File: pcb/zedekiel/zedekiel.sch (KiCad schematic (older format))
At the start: 150 parts, among them J2 USB_C_Receptacle_USB2.0, K1 KEYSW, K10 KEYSW, K11 KEYSW, K12 KEYSW, K13 KEYSW, K14 KEYSW, K15 KEYSW, K16 KEYSW, K17 KEYSW, K18 KEYSW, K19 KEYSW, K2 KEYSW, K20 KEYSW, K21 KEYSW, K22 KEYSW, K23 KEYSW, K24 KEYSW, K25 KEYSW, K26 KEYSW, K27 KEYSW, K28 KEYSW, K29 KEYSW, K3 KEYSW, K30 KEYSW, K31 KEYSW, K32 KEYSW, K33 KEYSW, K34 KEYSW, K35 KEYSW, K36 KEYSW, K37 KEYSW, K38 KEYSW, K39 KEYSW, K4 KEYSW, K40 KEYSW, K41 KEYSW, K42 KEYSW, K43 KEYSW, K44 KEYSW, K45 KEYSW, K46 KEYSW, K47 KEYSW, K48 KEYSW, K49 KEYSW, K5 KEYSW, K50 KEYSW, K51 KEYSW, K52 KEYSW, K53 KEYSW, K54 KEYSW, K55 KEYSW, K56 KEYSW, K57 KEYSW, K58 KEYSW, K59 KEYSW, K6 KEYSW, K60 KEYSW, K61 KEYSW, K62 KEYSW, K63 KEYSW, K64 KEYSW, K65 KEYSW, K66 KEYSW, K7 KEYSW, K8 KEYSW, K9 KEYSW, SW1 SW_PUSH, U1 ATmega16U4-AU_(modified), X1 16MHz

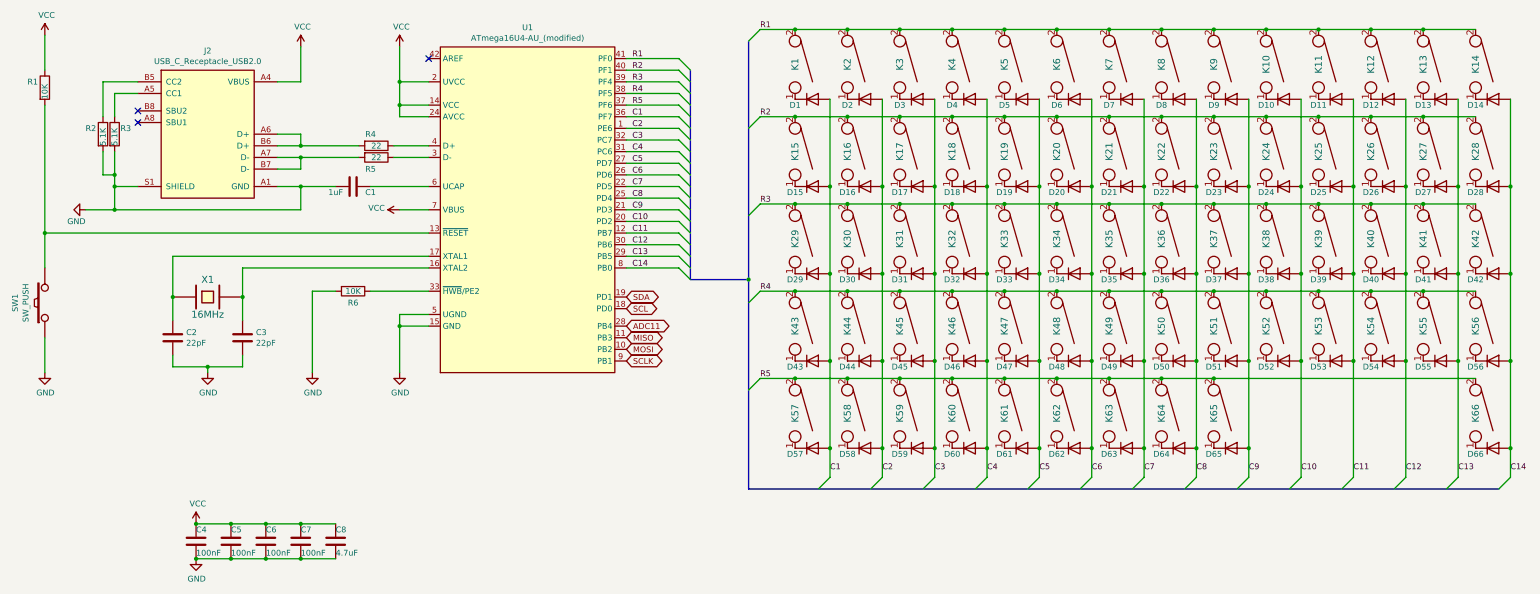
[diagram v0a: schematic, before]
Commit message: Diodes and sockets in place
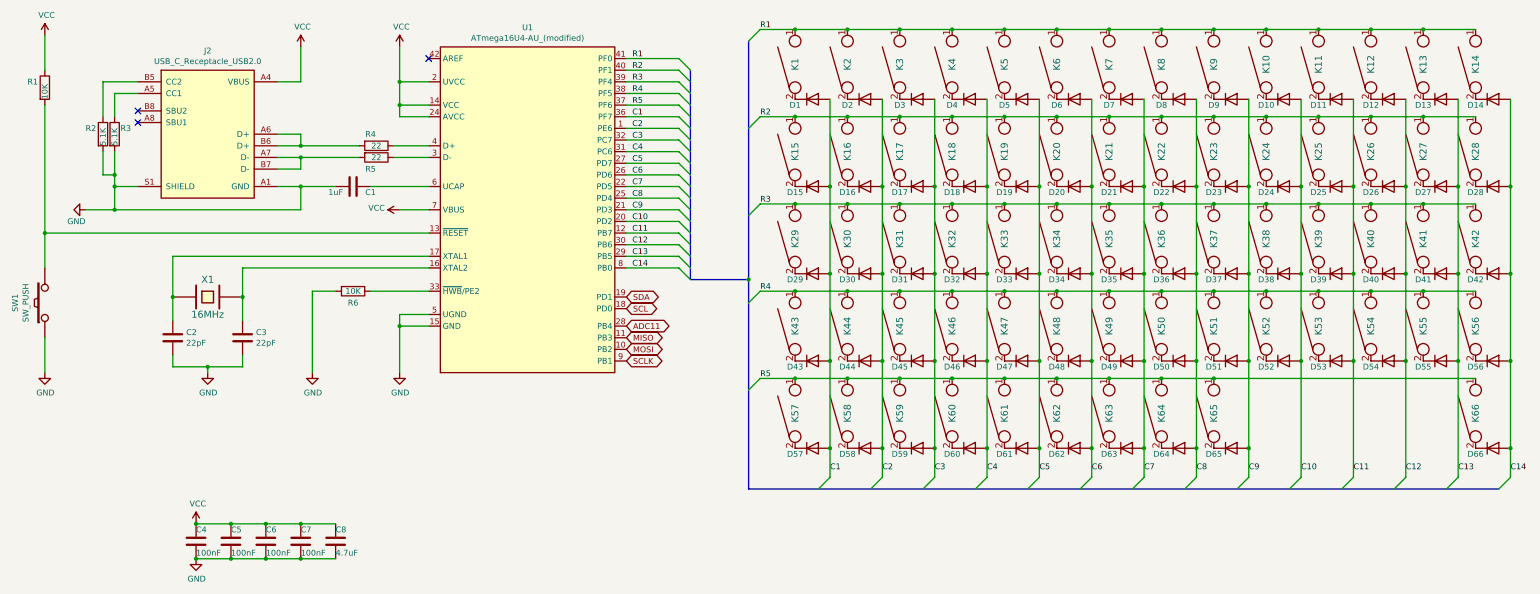
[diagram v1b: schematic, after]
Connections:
- net R1: now also K1.1, K10.1, K11.1, K12.1, K13.1, K14.1, K2.1, K3.1, K4.1, K5.1, K6.1, K7.1, K8.1, K9.1; no longer K1.2, K10.2, K11.2, K12.2, K13.2, K14.2, K2.2, K3.2, K4.2, K5.2, K6.2, K7.2, K8.2, K9.2
- net R2: now also K15.1, K16.1, K17.1, K18.1, K19.1, K20.1, K21.1, K22.1, K23.1, K24.1, K25.1, K26.1, K27.1, K28.1; no longer K15.2, K16.2, K17.2, K18.2, K19.2, K20.2, K21.2, K22.2, K23.2, K24.2, K25.2, K26.2, K27.2, K28.2
- net R3: now also K29.1, K30.1, K31.1, K32.1, K33.1, K34.1, K35.1, K36.1, K37.1, K38.1, K39.1, K40.1, K41.1, K42.1; no longer K29.2, K30.2, K31.2, K32.2, K33.2, K34.2, K35.2, K36.2, K37.2, K38.2, K39.2, K40.2, K41.2, K42.2
- net R4: now also K43.1, K44.1, K45.1, K46.1, K47.1, K48.1, K49.1, K50.1, K51.1, K52.1, K53.1, K54.1, K55.1, K56.1; no longer K43.2, K44.2, K45.2, K46.2, K47.2, K48.2, K49.2, K50.2, K51.2, K52.2, K53.2, K54.2, K55.2, K56.2
- net R5: now also K57.1, K58.1, K59.1, K60.1, K61.1, K62.1, K63.1, K64.1, K65.1, K66.1; no longer K57.2, K58.2, K59.2, K60.2, K61.2, K62.2, K63.2, K64.2, K65.2, K66.2
- net at D1.1 (K): now also K1.2; no longer K1.1
- net at D2.1 (K): now also K2.2; no longer K2.1
- net at D3.1 (K): now also K3.2; no longer K3.1
- net at D4.1 (K): now also K4.2; no longer K4.1
- net at D5.1 (K): now also K5.2; no longer K5.1
- net at D6.1 (K): now also K6.2; no longer K6.1
- net at D7.1 (K): now also K7.2; no longer K7.1
- net at D8.1 (K): now also K8.2; no longer K8.1
- net at D9.1 (K): now also K9.2; no longer K9.1
- net at D10.1 (K): now also K10.2; no longer K10.1
- net at D11.1 (K): now also K11.2; no longer K11.1
- net at D12.1 (K): now also K12.2; no longer K12.1
- net at D13.1 (K): now also K13.2; no longer K13.1
- net at D14.1 (K): now also K14.2; no longer K14.1
- net at D15.1 (K): now also K15.2; no longer K15.1
- net at D16.1 (K): now also K16.2; no longer K16.1
- net at D17.1 (K): now also K17.2; no longer K17.1
- net at D18.1 (K): now also K18.2; no longer K18.1
- net at D19.1 (K): now also K19.2; no longer K19.1
- net at D20.1 (K): now also K20.2; no longer K20.1
- net at D21.1 (K): now also K21.2; no longer K21.1
- net at D22.1 (K): now also K22.2; no longer K22.1
- net at D23.1 (K): now also K23.2; no longer K23.1
- net at D24.1 (K): now also K24.2; no longer K24.1
- net at D25.1 (K): now also K25.2; no longer K25.1
- net at D26.1 (K): now also K26.2; no longer K26.1
- net at D27.1 (K): now also K27.2; no longer K27.1
- net at D28.1 (K): now also K28.2; no longer K28.1
- net at D29.1 (K): now also K29.2; no longer K29.1
- net at D30.1 (K): now also K30.2; no longer K30.1
- net at D31.1 (K): now also K31.2; no longer K31.1
- net at D32.1 (K): now also K32.2; no longer K32.1
- net at D33.1 (K): now also K33.2; no longer K33.1
- net at D34.1 (K): now also K34.2; no longer K34.1
- net at D35.1 (K): now also K35.2; no longer K35.1
- net at D36.1 (K): now also K36.2; no longer K36.1
- net at D37.1 (K): now also K37.2; no longer K37.1
- net at D38.1 (K): now also K38.2; no longer K38.1
- net at D39.1 (K): now also K39.2; no longer K39.1
- net at D40.1 (K): now also K40.2; no longer K40.1
- net at D41.1 (K): now also K41.2; no longer K41.1
- net at D42.1 (K): now also K42.2; no longer K42.1
- net at D43.1 (K): now also K43.2; no longer K43.1
- net at D44.1 (K): now also K44.2; no longer K44.1
- net at D45.1 (K): now also K45.2; no longer K45.1
- net at D46.1 (K): now also K46.2; no longer K46.1
- net at D47.1 (K): now also K47.2; no longer K47.1
- net at D48.1 (K): now also K48.2; no longer K48.1
- net at D49.1 (K): now also K49.2; no longer K49.1
- net at D50.1 (K): now also K50.2; no longer K50.1
- net at D51.1 (K): now also K51.2; no longer K51.1
- net at D52.1 (K): now also K52.2; no longer K52.1
- net at D53.1 (K): now also K53.2; no longer K53.1
- net at D54.1 (K): now also K54.2; no longer K54.1
- net at D55.1 (K): now also K55.2; no longer K55.1
- net at D56.1 (K): now also K56.2; no longer K56.1
- net at D57.1 (K): now also K57.2; no longer K57.1
- net at D58.1 (K): now also K58.2; no longer K58.1
- net at D59.1 (K): now also K59.2; no longer K59.1
- net at D60.1 (K): now also K60.2; no longer K60.1
- net at D61.1 (K): now also K61.2; no longer K61.1
- net at D62.1 (K): now also K62.2; no longer K62.1
- net at D63.1 (K): now also K63.2; no longer K63.1
- net at D64.1 (K): now also K64.2; no longer K64.1
- net at D65.1 (K): now also K65.2; no longer K65.1
- net at D66.1 (K): now also K66.2; no longer K66.1
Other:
- moved on the sheet: K1, K10, K11, K12, K13, K14, K15, K16, K17, K18, K19, K2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

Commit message: Holes and stabilizers
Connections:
- net C1: no longer D57.2 (A)
- net C10: now also D62.2 (A)
- net C11: now also D63.2 (A)
- net C12: now also D64.2 (A)
- net C13: now also D65.2 (A)
- net C2: now also D57.2 (A); no longer D58.2 (A)
- net C3: no longer D59.2 (A)
- net C4: now also D58.2 (A); no longer D60.2 (A)
- net C5: now also D59.2 (A); no longer D61.2 (A)
- net C6: no longer D62.2 (A)
- net C7: now also D60.2 (A); no longer D63.2 (A)
- net C8: now also D61.2 (A); no longer D64.2 (A)
- net C9: no longer D65.2 (A)
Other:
- moved on the sheet: D57, D58, D59, D60, D61, D62, D63, D64, D65, K57, K58, K59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

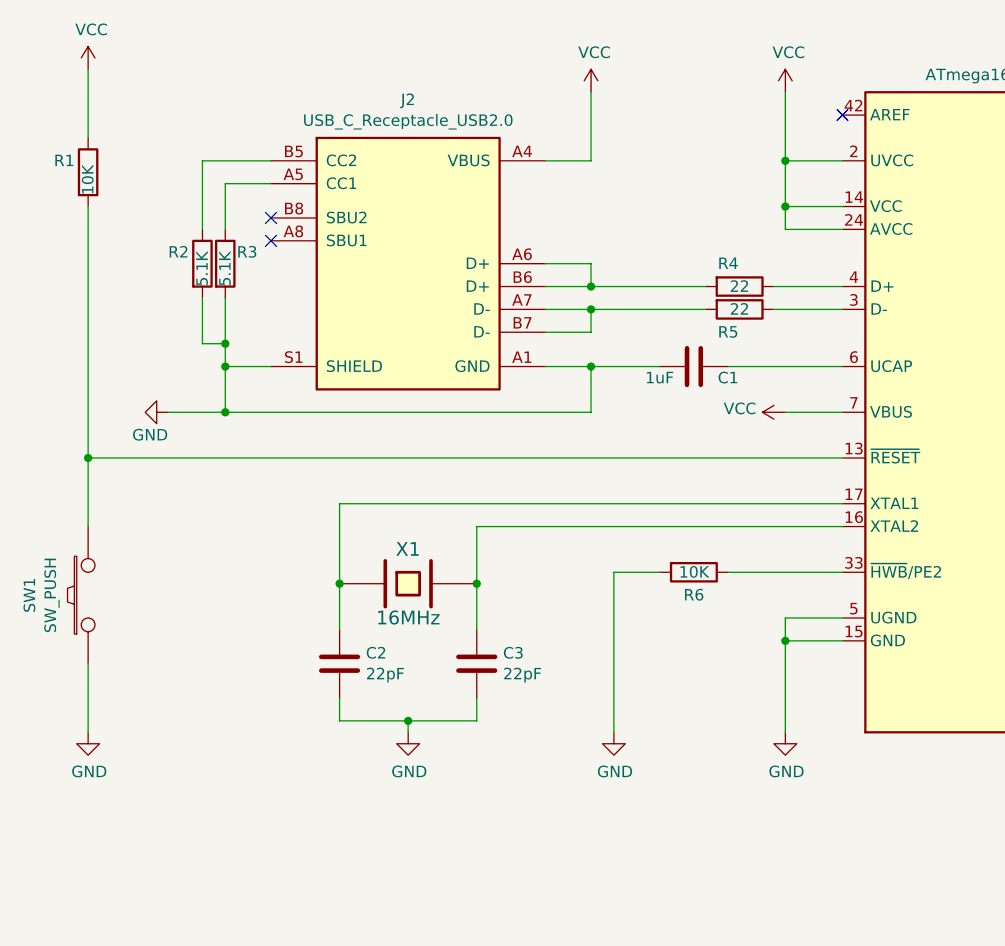
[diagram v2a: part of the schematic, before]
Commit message: Routing started.
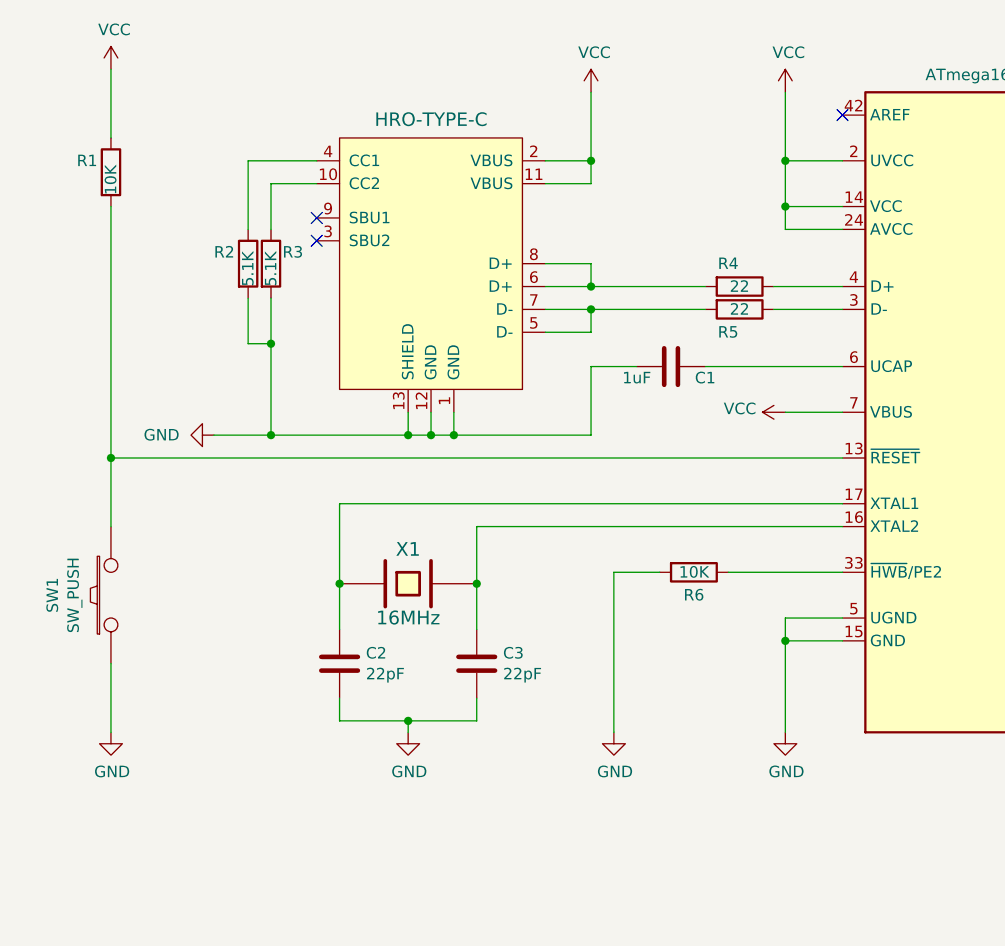
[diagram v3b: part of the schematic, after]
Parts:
- removed J2: USB_C_Receptacle_USB2.0, Connectors_USB:USB_C_Receptacle_Amphenol_12401548E4-2A, symbol usb_c_receptacle_usb2.0_modified:USB_C_Receptacle_USB2.0
- added USB?: HRO-TYPE-C, symbol hro-type-c_modified:HRO-TYPE-C
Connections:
- net GND: now also USB?.1 (GND), USB?.12 (GND), USB?.13 (SHIELD)
- net VCC: now also USB?.11 (VBUS), USB?.2 (VBUS)
- net at R3.1: now also USB?.10 (CC2)
- net at R2.1: now also USB?.4 (CC1)
- net at R4.2: now also USB?.6 (D+), USB?.8 (D+)
- net at R5.2: now also USB?.5 (D-), USB?.7 (D-)
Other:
- moved on the sheet: C1, R1, R2, R3, SW1
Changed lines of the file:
@@
 L Device:C C1
 U 1 1 5EE5A2F4
-P 3900 2450
-F 0 "C1" V 3950 2600 50  0000 C CNN
-F 1 "1uF" V 3950 2300 50  0000 C CNN
-F 2 "Capacitors_SMD:C_0603" H 3938 2300 50  0001 C CNN
-F 3 "~" H 3900 2450 50  0001 C CNN
-	1    3900 2450
+P 3800 2450
+F 0 "C1" V 3850 2600 50  0000 C CNN
+F 1 "1uF" V 3850 2300 50  0000 C CNN
+F 2 "Capacitors_SMD:C_0603" H 3838 2300 50  0001 C CNN
+F 3 "~" H 3800 2450 50  0001 C CNN
+	1    3800 2450
 	0    1    1    0
 $EndComp
 Wire Wire Line
-	4050 2450 4550 2450
-Wire Wire Line
-	3750 2450 3450 2450
-Wire Wire Line
-	3450 2650 3450 2450
-Connection ~ 3450 2450
-Wire Wire Line
-	3450 2450 3250 2450
+	3950 2450 4550 2450
 $Comp
 L keyboard_parts:SW_PUSH SW1
 U 1 1 5EE97D58
-P 1250 3450
-F 0 "SW1" H 1250 3705 50  0000 C CNN
-F 1 "SW_PUSH" H 1250 3614 50  0000 C CNN
-F 2 "custom:pad-button" H 1250 3450 60  0001 C CNN
-F 3 "" H 1250 3450 60  0000 C CNN
-	1    1250 3450
-	0    -1   -1   0
-$EndComp
-Wire Wire Line
-	1250 2850 1250 3150
+P 1350 3450
+F 0 "SW1" H 1350 3705 50  0000 C CNN
+F 1 "SW_PUSH" H 1350 3614 50  0000 C CNN
+F 2 "custom:pad-button" H 1350 3450 60  0001 C CNN
+F 3 "" H 1350 3450 60  0000 C CNN
+	1    1350 3450
+	0    -1   -1   0
+$EndComp
 $Comp
 L power:GND #PWR05
 U 1 1 5EEA1F4F
-P 1250 4050
-F 0 "#PWR05" H 1250 3800 50  0001 C CNN
-F 1 "GND" H 1255 3877 50  0000 C CNN
-F 2 "" H 1250 4050 50  0001 C CNN
-F 3 "" H 1250 4050 50  0001 C CNN
-	1    1250 4050
-	1    0    0    -1
-$EndComp
-Wire Wire Line
-	1250 3750 1250 4050
+P 1350 4050
+F 0 "#PWR05" H 1350 3800 50  0001 C CNN
+F 1 "GND" H 1355 3877 50  0000 C CNN
+F 2 "" H 1350 4050 50  0001 C CNN
+F 3 "" H 1350 4050 50  0001 C CNN
+	1    1350 4050
+	1    0    0    -1
+$EndComp
+Wire Wire Line
+	1350 3750 1350 4050
 $Comp
 L power:VCC #PWR01
 U 1 1 5EEA4CAF
-P 1250 1150
-F 0 "#PWR01" H 1250 1000 50  0001 C CNN
-F 1 "VCC" H 1265 1323 50  0000 C CNN
-F 2 "" H 1250 1150 50  0001 C CNN
-F 3 "" H 1250 1150 50  0001 C CNN
-	1    1250 1150
+P 1350 1150
+F 0 "#PWR01" H 1350 1000 50  0001 C CNN
+F 1 "VCC" H 1365 1323 50  0000 C CNN
+F 2 "" H 1350 1150 50  0001 C CNN
+F 3 "" H 1350 1150 50  0001 C CNN
+	1    1350 1150
 	1    0    0    -1
 $EndComp
@@
 L Device:R R1
 U 1 1 5EEB521E
-P 1250 1600
-F 0 "R1" H 1100 1650 50  0000 L CNN
-F 1 "10K" V 1250 1500 50  0000 L CNN
-F 2 "Resistors_SMD:R_0603" V 1180 1600 50  0001 C CNN
-F 3 "~" H 1250 1600 50  0001 C CNN
-	1    1250 1600
-	1    0    0    -1
-$EndComp
-Wire Wire Line
-	1250 1750 1250 2850
-Wire Wire Line
-	1250 1450 1250 1150
+P 1350 1600
+F 0 "R1" H 1200 1650 50  0000 L CNN
+F 1 "10K" V 1350 1500 50  0000 L CNN
+F 2 "Resistors_SMD:R_0603" V 1280 1600 50  0001 C CNN
+F 3 "~" H 1350 1600 50  0001 C CNN
+	1    1350 1600
+	1    0    0    -1
+$EndComp
+Wire Wire Line
+	1350 1450 1350 1150
 $Comp
 L power:GND #PWR04
 U 1 1 5EE60D7B
-P 1600 2650
-F 0 "#PWR04" H 1600 2400 50  0001 C CNN
-F 1 "GND" V 1700 2650 50  0000 R CNN
-F 2 "" H 1600 2650 50  0001 C CNN
-F 3 "" H 1600 2650 50  0001 C CNN
-	1    1600 2650
+P 1800 2750
+F 0 "#PWR04" H 1800 2500 50  0001 C CNN
+F 1 "GND" V 1800 2600 50  0000 R CNN
+F 2 "" H 1800 2750 50  0001 C CNN
+F 3 "" H 1800 2750 50  0001 C CNN
+	1    1800 2750
 	0    1    1    0
 $EndComp
@@
 	0    1    1    0
 $EndComp
-Connection ~ 1250 2850
-Wire Wire Line
-	1250 2850 4550 2850
 $Comp
 L power:GND #PWR06
@@
 Wire Wire Line
 	3450 5650 3150 5650
-$Comp
-L usb_c_receptacle_usb2.0_modified:USB_C_Receptacle_USB2.0 J2
-U 1 1 6061B4FB
-P 2650 2000
-F 0 "J2" H 2650 2717 50  0000 C CNN
-F 1 "USB_C_Receptacle_USB2.0" H 2650 2626 50  0000 C CNN
-F 2 "Connectors_USB:USB_C_Receptacle_Amphenol_12401548E4-2A" H 2800 1850 50  0001 C CNN
-F 3 "https://www.usb.org/sites/default/files/documents/usb_type-c.zip" H 2800 1850 50  0001 C CNN
-	1    2650 2000
-	1    0    0    -1
-$EndComp
-Wire Wire Line
-	2050 1550 1750 1550
-Wire Wire Line
-	2050 1650 1850 1650
-NoConn ~ 2050 1800
-NoConn ~ 2050 1900
-Wire Wire Line
-	3250 2000 3450 2000
-Wire Wire Line
-	3450 2000 3450 2100
-Wire Wire Line
-	3450 2100 3250 2100
+Wire Wire Line
+	2250 1550 1950 1550
+Wire Wire Line
+	2250 1650 2050 1650
+NoConn ~ 2250 1800
+NoConn ~ 2250 1900
 Wire Wire Line
 	3250 2200 3450 2200
@@
 	3450 2200 3950 2200
 Connection ~ 3450 2200
-Wire Wire Line
-	3950 2100 3450 2100
-Connection ~ 3450 2100
 Wire Wire Line
 	3250 1550 3450 1550
@@
 $EndComp
 Wire Wire Line
-	1750 1550 1750 1850
+	1950 1550 1950 1850
 $Comp
 L Device:R R2
 U 1 1 5EE7E2CD
-P 1750 2000
-F 0 "R2" H 1600 2050 50  0000 L CNN
-F 1 "5.1K" V 1750 1900 50  0000 L CNN
-F 2 "Resistors_SMD:R_0603" V 1680 2000 50  0001 C CNN
-F 3 "~" H 1750 2000 50  0001 C CNN
-	1    1750 2000
-	1    0    0    -1
-$EndComp
-Wire Wire Line
-	1850 1650 1850 1850
+P 1950 2000
+F 0 "R2" H 1800 2050 50  0000 L CNN
+F 1 "5.1K" V 1950 1900 50  0000 L CNN
+F 2 "Resistors_SMD:R_0603" V 1880 2000 50  0001 C CNN
+F 3 "~" H 1950 2000 50  0001 C CNN
+	1    1950 2000
+	1    0    0    -1
+$EndComp
+Wire Wire Line
+	2050 1650 2050 1850
 $Comp
 L Device:R R3
 U 1 1 5EE7DBB6
-P 1850 2000
-F 0 "R3" H 1900 2050 50  0000 L CNN
-F 1 "5.1K" V 1850 1900 50  0000 L CNN
-F 2 "Resistors_SMD:R_0603" V 1780 2000 50  0001 C CNN
-F 3 "~" H 1850 2000 50  0001 C CNN
-	1    1850 2000
-	1    0    0    -1
-$EndComp
-Wire Wire Line
-	1850 2150 1850 2350
-Wire Wire Line
-	1750 2150 1750 2350
-Wire Wire Line
-	1750 2350 1850 2350
-Wire Wire Line
-	2050 2450 1850 2450
-Wire Wire Line
-	1850 2450 1850 2650
-Connection ~ 1850 2650
-Wire Wire Line
-	1850 2650 3450 2650
-Wire Wire Line
-	1850 2350 1850 2450
-Connection ~ 1850 2350
-Connection ~ 1850 2450
-Wire Wire Line
-	1850 2650 1600 2650
+P 2050 2000
+F 0 "R3" H 2100 2050 50  0000 L CNN
+F 1 "5.1K" V 2050 1900 50  0000 L CNN
+F 2 "Resistors_SMD:R_0603" V 1980 2000 50  0001 C CNN
+F 3 "~" H 2050 2000 50  0001 C CNN
+	1    2050 2000
+	1    0    0    -1
+$EndComp
+Wire Wire Line
+	2050 2150 2050 2350
+Wire Wire Line
+	1950 2150 1950 2350
+Wire Wire Line
+	1950 2350 2050 2350
+Connection ~ 2050 2350
 $Comp
 L keyboard_parts:KEYSW K12
@@
 Wire Wire Line
 	9500 4100 10400 4100
+Connection ~ 3450 2100
+Wire Wire Line
+	3950 2100 3450 2100
+Wire Wire Line
+	3450 2100 3250 2100
+Wire Wire Line
+	3450 2000 3450 2100
+Wire Wire Line
+	3250 2000 3450 2000
+$Comp
+L hro-type-c_modified:HRO-TYPE-C USB?
+U 1 1 5EF51AB7
+P 3150 2050
+F 0 "USB?" H 2750 2050 60  0001 C CNN
+F 1 "HRO-TYPE-C" H 2750 2730 59  0000 C CNN
+F 2 "" H 3150 2050 60  0001 C CNN
+F 3 "" H 3150 2050 60  0001 C CNN
+	1    3150 2050
+	1    0    0    -1
+$EndComp
+Wire Wire Line
+	3250 1650 3450 1650
+Wire Wire Line
+	3450 1650 3450 1550
+Connection ~ 3450 1550
+Wire Wire Line
+	2050 2350 2050 2750
+Wire Wire Line
+	3650 2450 3450 2450
+Wire Wire Line
+	3450 2450 3450 2750
+Wire Wire Line
+	3450 2750 2850 2750
+Wire Wire Line
+	2850 2650 2850 2750
+Connection ~ 2850 2750
+Wire Wire Line
+	2850 2750 2750 2750
+Wire Wire Line
+	2750 2650 2750 2750
+Connection ~ 2750 2750
+Wire Wire Line
+	2750 2750 2650 2750
+Wire Wire Line
+	2650 2650 2650 2750
+Connection ~ 2650 2750
+Wire Wire Line
+	2650 2750 2050 2750
+Connection ~ 2050 2750
+Wire Wire Line
+	2050 2750 1800 2750
+Wire Wire Line
+	1350 1750 1350 2850
+Wire Wire Line
+	4550 2850 1350 2850
 Wire Bus Line
 	7300 1200 7300 3250
@@
 Wire Bus Line
 	6800 1450 6800 3250
+Connection ~ 1350 2850
+Wire Wire Line
+	1350 2850 1350 3150
 $EndSCHEMATC

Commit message: Routing. Fixed a moved socket.
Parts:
- USB1: renamed from USB?; footprint (none) -> Type-C:HRO-TYPE-C-31-M-12
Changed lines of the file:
@@
 	3250 2000 3450 2000
 $Comp
-L hro-type-c_modified:HRO-TYPE-C USB?
+L hro-type-c_modified:HRO-TYPE-C USB1
 U 1 1 5EF51AB7
 P 3150 2050
-F 0 "USB?" H 2750 2050 60  0001 C CNN
+F 0 "USB1" H 2750 2050 60  0001 C CNN
 F 1 "HRO-TYPE-C" H 2750 2730 59  0000 C CNN
-F 2 "" H 3150 2050 60  0001 C CNN
+F 2 "Type-C:HRO-TYPE-C-31-M-12" H 3150 2050 60  0001 C CNN
 F 3 "" H 3150 2050 60  0001 C CNN
 	1    3150 2050
